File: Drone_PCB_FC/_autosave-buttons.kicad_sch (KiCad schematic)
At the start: 5 parts, among them U3 W25Q128JVSIQTR

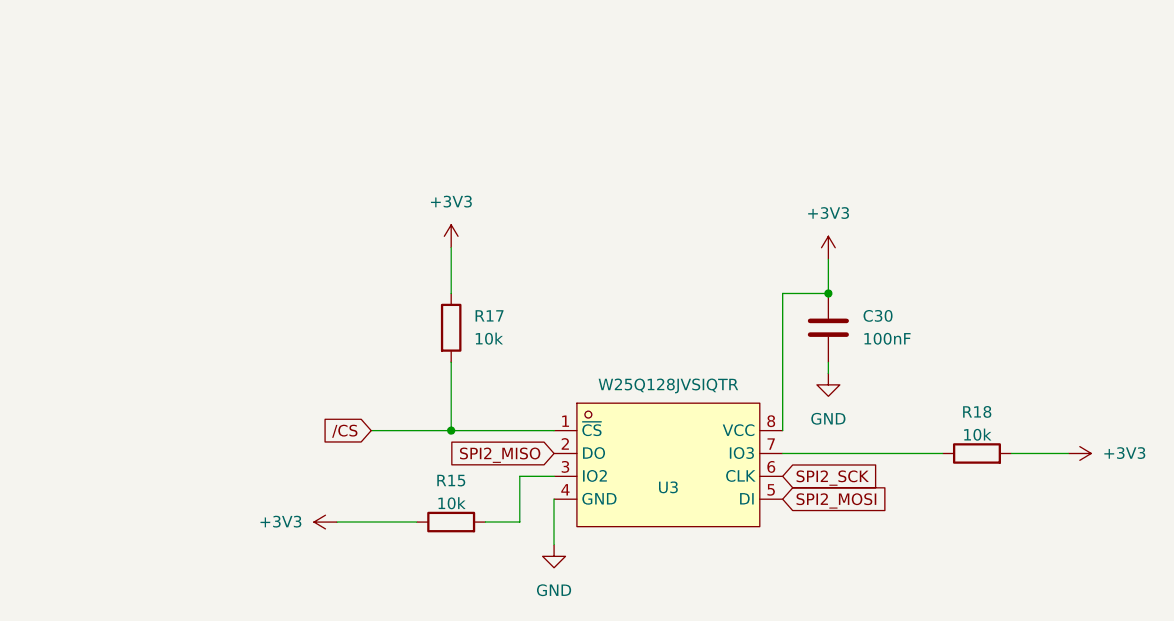
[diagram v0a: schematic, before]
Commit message: pcb is 'done' but i think i messed up the IMU so ill fix later
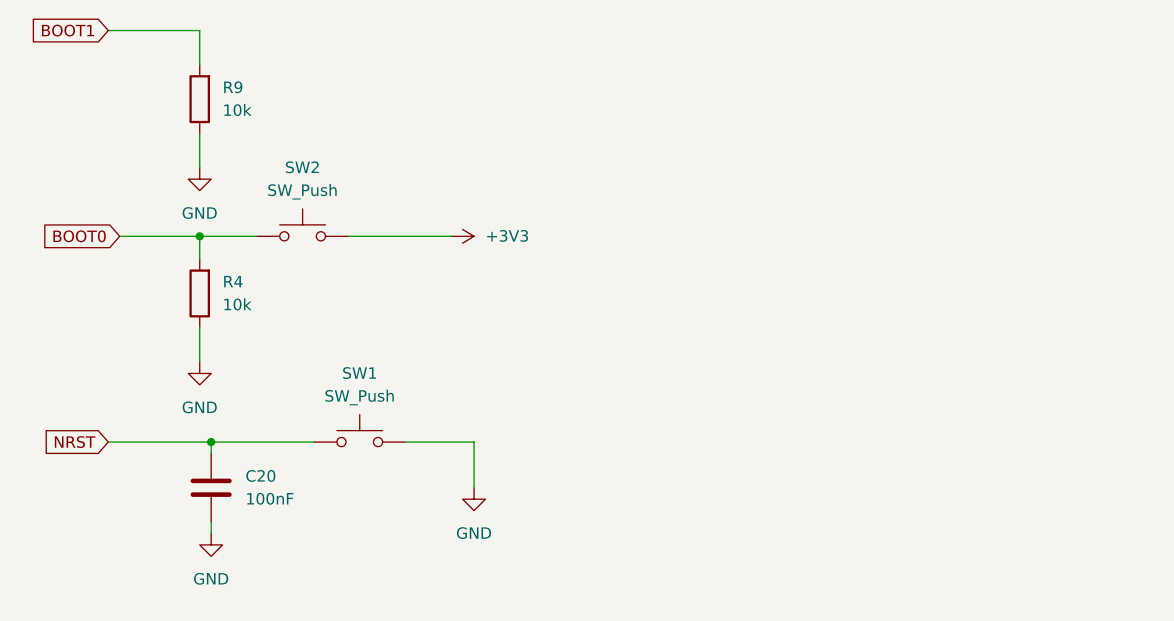
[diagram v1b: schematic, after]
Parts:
- removed C30: 100nF, Capacitor_SMD:C_0805_2012Metric, symbol Device:C
- removed R15, R17, R18: 10k, Resistor_SMD:R_0805_2012Metric, symbol Device:R
- removed U3: W25Q128JVSIQTR, drone_lib:SOIC-8_L5.3-W5.3-P1.27-LS8.0-BL, symbol drone_lib:W25Q128JVSIQTR
- added C20: 100nF, Capacitor_SMD:C_0805_2012Metric, symbol Device:C
- added R4, R9: 10k, Resistor_SMD:R_0805_2012Metric, symbol Device:R
- added SW1, SW2: SW_Push, Button_Switch_THT:SW_PUSH_6mm, symbol Switch:SW_Push
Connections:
- net +3V3: now also SW2.2
- net GND: now also C20.2, R4.1, R9.1, SW1.2
- new net BOOT0: R4.2, SW2.1
- new net BOOT1: R9.2
- new net NRST: C20.1, SW1.1
